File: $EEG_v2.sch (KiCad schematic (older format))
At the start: 5 parts, among them P1 CONN_5, P2 CONN_1, P3 CONN_1, P4 USB_A, SW1 SPST

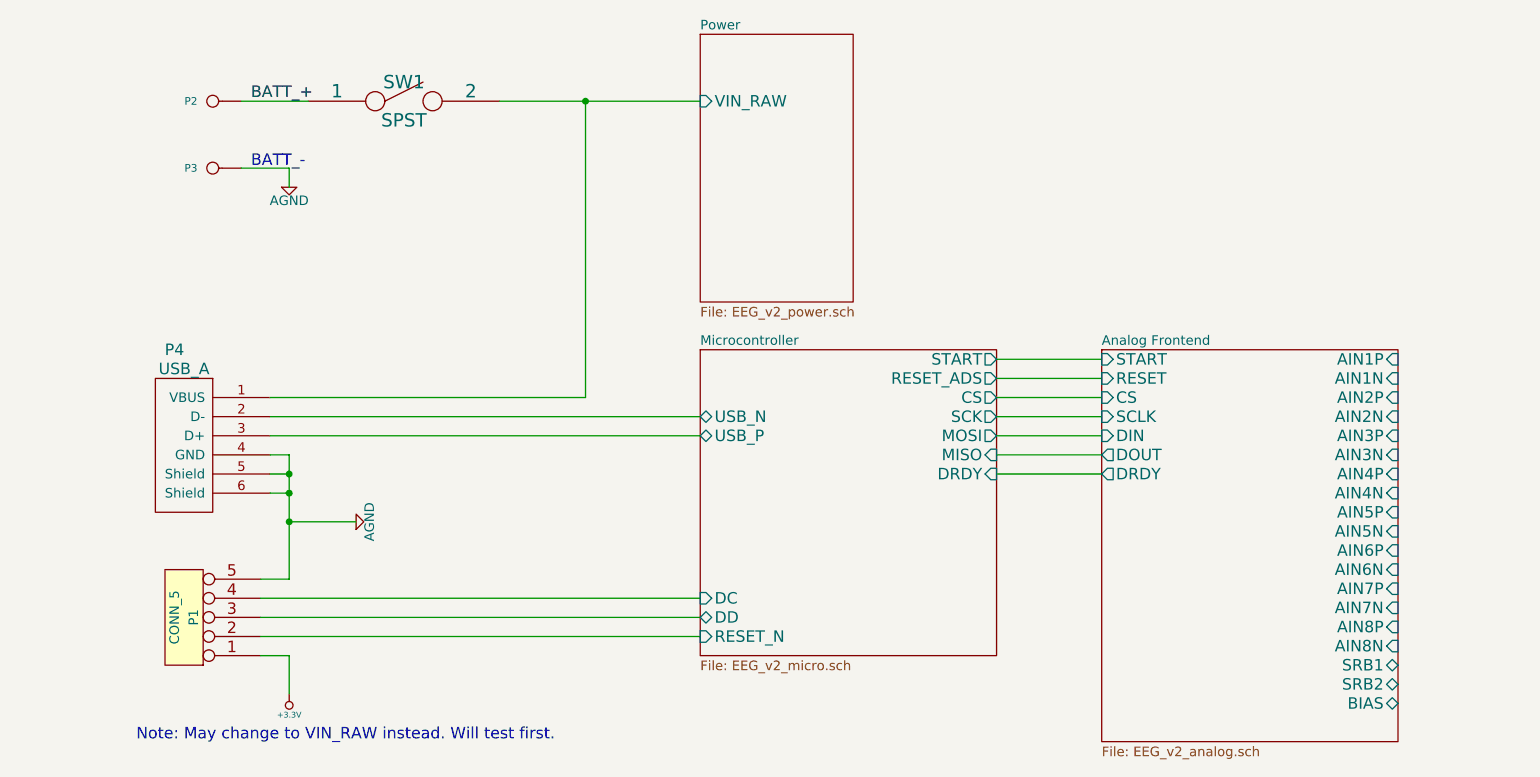
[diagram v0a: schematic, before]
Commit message: Add pin headers for electrodes and debug signals.
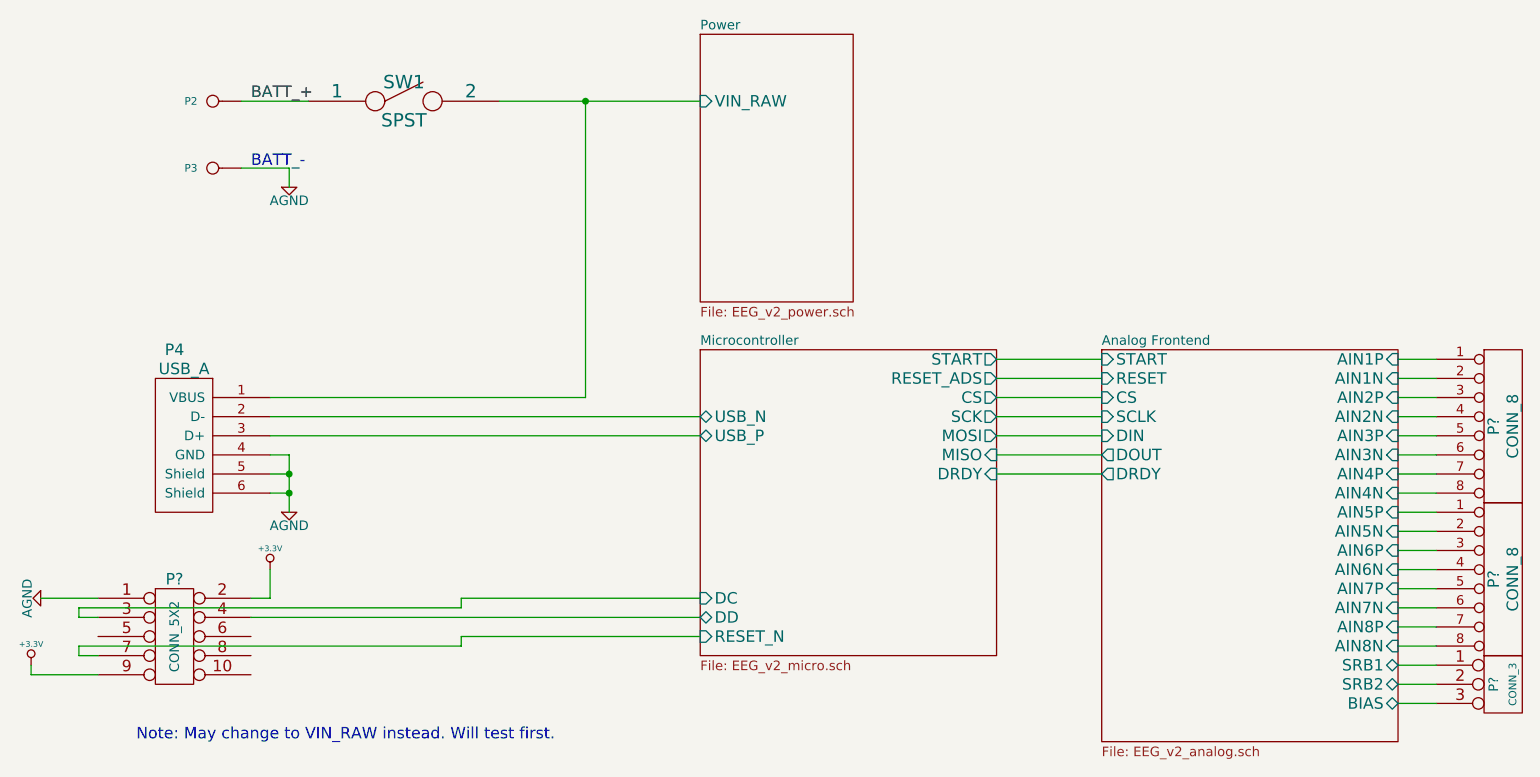
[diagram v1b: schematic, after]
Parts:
- removed P1: CONN_5, ~, symbol CONN_5
- added P? (x2): CONN_8, ~, symbol CONN_8
- added P?: CONN_3, ~, symbol CONN_3
- added P?: CONN_5X2, ~, symbol CONN_5X2
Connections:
- net +3.3V: now also P?.2, P?.9
- net AGND: now also P?.1
- net Analog Frontend/AIN1N: now also P?.2 (P2)
- net Analog Frontend/AIN1P: now also P?.1 (P1)
- net Analog Frontend/AIN2N: now also P?.4 (P4)
- net Analog Frontend/AIN2P: now also P?.3 (P3)
- net Analog Frontend/AIN3N: now also P?.6 (P6)
- net Analog Frontend/AIN3P: now also P?.5 (P5)
- net Analog Frontend/AIN4N: now also P?.8 (P8)
- net Analog Frontend/AIN4P: now also P?.7 (P7)
- net Analog Frontend/AIN5N: now also P?.2 (P2)
- net Analog Frontend/AIN5P: now also P?.1 (P1)
- net Analog Frontend/AIN6N: now also P?.4 (P4)
- net Analog Frontend/AIN6P: now also P?.3 (P3)
- net Analog Frontend/AIN7N: now also P?.6 (P6)
- net Analog Frontend/AIN7P: now also P?.5 (P5)
- net Analog Frontend/AIN8N: now also P?.8 (P8)
- net Analog Frontend/AIN8P: now also P?.7 (P7)
- net Analog Frontend/BIAS: now also P?.3 (P3)
- net Analog Frontend/SRB1: now also P?.1 (P1)
- net Analog Frontend/SRB2: now also P?.2 (PM)
- net Microcontroller/DC: now also P?.3
- net Microcontroller/DD: now also P?.4
- net Microcontroller/RESET_N: now also P?.7
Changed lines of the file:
@@
 	2650 4750 2750 4750
-Wire Wire Line
-	2750 4750 2750 5400
 Wire Wire Line
 	2650 4850 2750 4850
 Connection ~ 2750 4850
 Wire Wire Line
-	2650 4950 2750 4950
+	2750 4950 2650 4950
 Connection ~ 2750 4950
 $Comp
 L AGND #PWR01
 U 1 1 54C3BF39
-P 3100 5100
-F 0 "#PWR01" H 3100 5100 40  0001 C CNN
-F 1 "AGND" H 3100 5030 50  0000 C CNN
-F 2 "~" H 3100 5100 60  0000 C CNN
-F 3 "~" H 3100 5100 60  0000 C CNN
-	1    3100 5100
-	0    -1   -1   0
+P 2750 5050
+F 0 "#PWR01" H 2750 5050 40  0001 C CNN
+F 1 "AGND" H 2750 4980 50  0000 C CNN
+F 2 "~" H 2750 5050 60  0000 C CNN
+F 3 "~" H 2750 5050 60  0000 C CNN
+	1    2750 5050
+	1    0    0    -1
 $EndComp
 $Comp
@@
 Text Notes 2550 3250 0    60   ~ 0
 BATT_-
-$Comp
-L CONN_5 P1
-U 1 1 54C4DEF5
-P 2200 5600
-F 0 "P1" V 2150 5600 50  0000 C CNN
-F 1 "CONN_5" V 2250 5600 50  0000 C CNN
-F 2 "~" H 2200 5600 60  0000 C CNN
-F 3 "~" H 2200 5600 60  0000 C CNN
-	1    2200 5600
-	-1   0    0    1
-$EndComp
-Wire Wire Line
-	2750 5400 2600 5400
-Wire Wire Line
-	2750 5100 3100 5100
-Connection ~ 2750 5100
-Wire Wire Line
-	2600 5500 4900 5500
-Wire Wire Line
-	2600 5600 4900 5600
-Wire Wire Line
-	4900 5700 2600 5700
-Wire Wire Line
-	2600 5800 2750 5800
-Wire Wire Line
-	2750 5800 2750 6000
+Wire Wire Line
+	2550 5600 4900 5600
+Wire Wire Line
+	4900 5700 3650 5700
 $Comp
 L +3.3V #PWR03
 U 1 1 54C4F12C
-P 2750 6000
-F 0 "#PWR03" H 2750 5960 30  0001 C CNN
-F 1 "+3.3V" H 2750 6110 30  0000 C CNN
-F 2 "~" H 2750 6000 60  0000 C CNN
-F 3 "~" H 2750 6000 60  0000 C CNN
-	1    2750 6000
-	-1   0    0    1
+P 2650 5350
+F 0 "#PWR03" H 2650 5310 30  0001 C CNN
+F 1 "+3.3V" H 2650 5460 30  0000 C CNN
+F 2 "~" H 2650 5350 60  0000 C CNN
+F 3 "~" H 2650 5350 60  0000 C CNN
+	1    2650 5350
+	1    0    0    -1
 $EndComp
 Text Notes 1950 6250 0    60   ~ 0
 Note: May change to VIN_RAW instead. Will test first.
+$Comp
+L CONN_8 P?
+U 1 1 54C84F21
+P 9100 4600
+F 0 "P?" V 9050 4600 60  0000 C CNN
+F 1 "CONN_8" V 9150 4600 60  0000 C CNN
+F 2 "~" H 9100 4600 60  0000 C CNN
+F 3 "~" H 9100 4600 60  0000 C CNN
+	1    9100 4600
+	1    0    0    -1
+$EndComp
+$Comp
+L CONN_8 P?
+U 1 1 54C84F2E
+P 9100 5400
+F 0 "P?" V 9050 5400 60  0000 C CNN
+F 1 "CONN_8" V 9150 5400 60  0000 C CNN
+F 2 "~" H 9100 5400 60  0000 C CNN
+F 3 "~" H 9100 5400 60  0000 C CNN
+	1    9100 5400
+	1    0    0    -1
+$EndComp
+$Comp
+L CONN_3 P?
+U 1 1 54C84FBA
+P 9100 5950
+F 0 "P?" V 9050 5950 50  0000 C CNN
+F 1 "CONN_3" V 9150 5950 40  0000 C CNN
+F 2 "~" H 9100 5950 60  0000 C CNN
+F 3 "~" H 9100 5950 60  0000 C CNN
+	1    9100 5950
+	1    0    0    -1
+$EndComp
+Wire Wire Line
+	8550 4250 8750 4250
+Wire Wire Line
+	8750 4350 8550 4350
+Wire Wire Line
+	8550 4450 8750 4450
+Wire Wire Line
+	8750 4550 8550 4550
+Wire Wire Line
+	8550 4650 8750 4650
+Wire Wire Line
+	8750 4750 8550 4750
+Wire Wire Line
+	8550 4850 8750 4850
+Wire Wire Line
+	8750 4950 8550 4950
+Wire Wire Line
+	8550 5050 8750 5050
+Wire Wire Line
+	8750 5150 8550 5150
+Wire Wire Line
+	8550 5250 8750 5250
+Wire Wire Line
+	8750 5350 8550 5350
+Wire Wire Line
+	8550 5450 8750 5450
+Wire Wire Line
+	8750 5550 8550 5550
+Wire Wire Line
+	8550 5650 8750 5650
+Wire Wire Line
+	8750 5750 8550 5750
+Wire Wire Line
+	8550 5850 8750 5850
+Wire Wire Line
+	8750 5950 8550 5950
+Wire Wire Line
+	8550 6050 8750 6050
+$Comp
+L CONN_5X2 P?
+U 1 1 54C8BF12
+P 2150 5700
+F 0 "P?" H 2150 6000 60  0000 C CNN
+F 1 "CONN_5X2" V 2150 5700 50  0000 C CNN
+F 2 "~" H 2150 5700 60  0000 C CNN
+F 3 "~" H 2150 5700 60  0000 C CNN
+	1    2150 5700
+	1    0    0    -1
+$EndComp
+Wire Wire Line
+	2750 4750 2750 5050
+$Comp
+L AGND #PWR?
+U 1 1 54C8DF7C
+P 1450 5500
+F 0 "#PWR?" H 1450 5500 40  0001 C CNN
+F 1 "AGND" H 1450 5430 50  0000 C CNN
+F 2 "~" H 1450 5500 60  0000 C CNN
+F 3 "~" H 1450 5500 60  0000 C CNN
+	1    1450 5500
+	0    1    1    0
+$EndComp
+Wire Wire Line
+	1650 5550 3650 5550
+Wire Wire Line
+	1650 5550 1650 5600
+Wire Wire Line
+	1650 5600 1750 5600
+Wire Wire Line
+	3650 5550 3650 5500
+Wire Wire Line
+	3650 5500 4900 5500
+Wire Wire Line
+	2550 5500 2650 5500
+Wire Wire Line
+	2650 5500 2650 5350
+Wire Wire Line
+	1750 5500 1450 5500
+Wire Wire Line
+	3650 5700 3650 5750
+Wire Wire Line
+	3650 5750 1650 5750
+Wire Wire Line
+	1650 5750 1650 5800
+Wire Wire Line
+	1650 5800 1750 5800
+$Comp
+L +3.3V #PWR?
+U 1 1 54C95C9F
+P 1400 5850
+F 0 "#PWR?" H 1400 5810 30  0001 C CNN
+F 1 "+3.3V" H 1400 5960 30  0000 C CNN
+F 2 "~" H 1400 5850 60  0000 C CNN
+F 3 "~" H 1400 5850 60  0000 C CNN
+	1    1400 5850
+	1    0    0    -1
+$EndComp
+Wire Wire Line
+	1750 5900 1400 5900
+Wire Wire Line
+	1400 5900 1400 5850
 $EndSCHEMATC
